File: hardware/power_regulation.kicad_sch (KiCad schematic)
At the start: 19 parts, among them U3 MAX6106, U4 LM27761

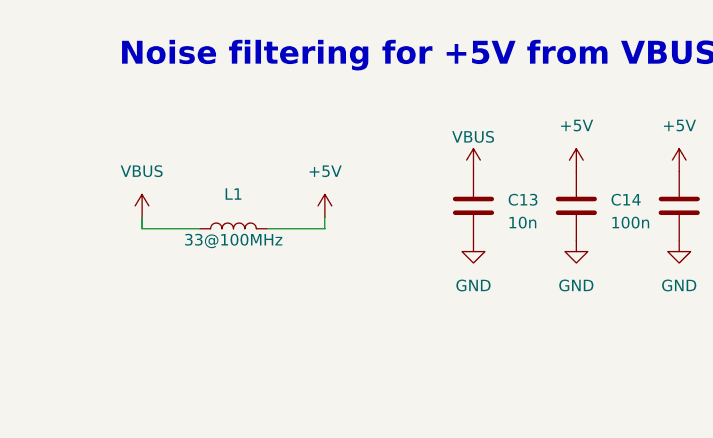
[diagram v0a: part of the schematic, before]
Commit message: finalize pcb design; add layout file
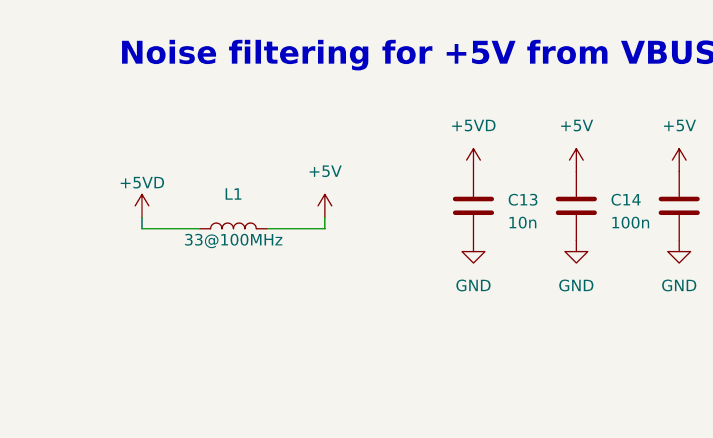
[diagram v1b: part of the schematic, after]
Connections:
- net VBUS renamed +5VD
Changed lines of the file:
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@@
   (title_block
     (title "Power regulation")
-    (date "2023-08-08")
+    (date "2023-08-15")
     (company "bitgloo")
     (comment 1 "Released under the CERN Open Hardware Licence Version 2 - Strongly Reciprocal")
@@
     )
   )
-  (symbol (lib_id "power:VBUS") (at 96.52 66.04 0) (unit 1)
-    (in_bom yes) (on_board yes) (dnp no) (fields_autoplaced)
-    (property "Reference" "#PWR061" (at 96.52 69.85 0)
-      (effects (font (size 1.27 1.27)) hide)
-    )
-    (property "Value" "VBUS" (at 96.52 62.23 0)
-      (effects (font (size 1.27 1.27)))
-    )
-    (property "Footprint" "" (at 96.52 66.04 0)
-      (effects (font (size 1.27 1.27)) hide)
-    )
-    (property "Datasheet" "" (at 96.52 66.04 0)
-      (effects (font (size 1.27 1.27)) hide)
-    )
-    (pin "1")
-    (instances
-      (project "DSP PAW add-on board"
-        (path "/c291319b-d76e-4fda-91cc-061acff65f9f/270d19d2-3af2-41db-ad1c-33373417ec82"
-          (reference "#PWR061") (unit 1)
-        )
-        (path "/c291319b-d76e-4fda-91cc-061acff65f9f/97fc232a-dbc7-49da-a6a0-e33e9aacbabd"
-          (reference "#PWR017") (unit 1)
-        )
-      )
-    )
-  )
   (symbol (lib_id "power:VDDA") (at 222.25 134.62 0) (unit 1)
     (in_bom yes) (on_board yes) (dnp no) (fields_autoplaced)
@@
         (path "/c291319b-d76e-4fda-91cc-061acff65f9f/97fc232a-dbc7-49da-a6a0-e33e9aacbabd"
           (reference "TP3") (unit 1)
-        )
-      )
-    )
-  )
-  (symbol (lib_id "power:VBUS") (at 59.69 71.12 0) (unit 1)
-    (in_bom yes) (on_board yes) (dnp no)
-    (property "Reference" "#PWR022" (at 59.69 74.93 0)
-      (effects (font (size 1.27 1.27)) hide)
-    )
-    (property "Value" "VBUS" (at 59.69 66.04 0)
-      (effects (font (size 1.27 1.27)))
-    )
-    (property "Footprint" "" (at 59.69 71.12 0)
-      (effects (font (size 1.27 1.27)) hide)
-    )
-    (property "Datasheet" "" (at 59.69 71.12 0)
-      (effects (font (size 1.27 1.27)) hide)
-    )
-    (pin "1")
-    (instances
-      (project "DSP PAW add-on board"
-        (path "/c291319b-d76e-4fda-91cc-061acff65f9f/97fc232a-dbc7-49da-a6a0-e33e9aacbabd"
-          (reference "#PWR022") (unit 1)
         )
       )
@@
     )
   )
+  (symbol (lib_id "power:+5VD") (at 96.52 66.04 0) (unit 1)
+    (in_bom yes) (on_board yes) (dnp no)
+    (property "Reference" "#PWR017" (at 96.52 69.85 0)
+      (effects (font (size 1.27 1.27)) hide)
+    )
+    (property "Value" "+5VD" (at 96.52 60.96 0)
+      (effects (font (size 1.27 1.27)))
+    )
+    (property "Footprint" "" (at 96.52 66.04 0)
+      (effects (font (size 1.27 1.27)) hide)
+    )
+    (property "Datasheet" "" (at 96.52 66.04 0)
+      (effects (font (size 1.27 1.27)) hide)
+    )
+    (pin "1")
+    (instances
+      (project "DSP PAW add-on board"
+        (path "/c291319b-d76e-4fda-91cc-061acff65f9f/97fc232a-dbc7-49da-a6a0-e33e9aacbabd"
+          (reference "#PWR017") (unit 1)
+        )
+      )
+    )
+  )
   (symbol (lib_id "power:+5V") (at 198.12 64.77 0) (unit 1)
     (in_bom yes) (on_board yes) (dnp no) (fields_autoplaced)
@@
         )
       )
+    )
+  )
+  (symbol (lib_id "power:+5VD") (at 59.69 71.12 0) (unit 1)
+    (in_bom yes) (on_board yes) (dnp no) (fields_autoplaced)
+    (property "Reference" "#PWR022" (at 59.69 74.93 0)
+      (effects (font (size 1.27 1.27)) hide)
+    )
+    (property "Value" "+5VD" (at 59.69 67.31 0)
+      (effects (font (size 1.27 1.27)))
+    )
+    (property "Footprint" "" (at 59.69 71.12 0)
+      (effects (font (size 1.27 1.27)) hide)
+    )
+    (property "Datasheet" "" (at 59.69 71.12 0)
+      (effects (font (size 1.27 1.27)) hide)
+    )
+    (pin "1")
+    (instances
+      (project "DSP PAW add-on board"
+        (path "/c291319b-d76e-4fda-91cc-061acff65f9f/97fc232a-dbc7-49da-a6a0-e33e9aacbabd"
+          (reference "#PWR022") (unit 1)
+        )
+      )

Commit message: pcb design finalization
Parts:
- C13: LCSC Part # (none) -> C57112
- C14: LCSC Part # (none) -> C14663
- C15, C16, C18, C21: LCSC Part # (none) -> C19666
- C17, C20: LCSC Part # (none) -> C15849
- C19: LCSC Part # (none) -> C23630
- L1: LCSC Part # (none) -> C88984
- R19: value 174k -> 174k/1%; LCSC Part # (none) -> C482778
- R20: LCSC Part # (none) -> C21189
- R21: value 56k -> 56k/1%; LCSC Part # (none) -> C5140721
- TP1, TP2, TP3, TP4: DNP (none) -> T
- U3: LCSC Part # (none) -> C26804; Part Number MAX6106EUR+T -> REF3020AIDBZR
- U4: LCSC Part # (none) -> C129351
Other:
- note added: "Can substitute REF3020"
- title: Power regulation -> DSP PAW add-on board
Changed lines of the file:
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@@
   (paper "A4")
   (title_block
-    (title "Power regulation")
-    (date "2023-08-15")
+    (title "DSP PAW add-on board")
+    (date "2023-08-18")
     (company "bitgloo")
     (comment 1 "Released under the CERN Open Hardware Licence Version 2 - Strongly Reciprocal")
@@
     (effects (font (size 2.54 2.54) (thickness 0.254) bold) (justify left bottom))
   )
+  (text "Can substitute REF3020" (at 170.18 78.74 0)
+    (effects (font (size 1.27 1.27)) (justify left bottom))
+  )
   (text "Noise filtering for +5V from VBUS" (at 57.15 54.61 0)
     (effects (font (size 2.54 2.54) (thickness 0.254) bold) (justify left bottom))
@@
       (effects (font (size 1.27 1.27)) hide)
     )
+    (property "DNP" "T" (at 204.47 134.62 0)
+      (effects (font (size 1.27 1.27)) hide)
+    )
+    (property "LCSC Part #" "" (at 204.47 134.62 0)
+      (effects (font (size 1.27 1.27)) hide)
+    )
     (pin "1")
     (instances
@@
     )
     (property "Part Number" "CL10A475KP8NNNC" (at 118.11 135.89 0)
+      (effects (font (size 1.27 1.27)) hide)
+    )
+    (property "DNP" "" (at 118.11 135.89 0)
+      (effects (font (size 1.27 1.27)) hide)
+    )
+    (property "LCSC Part #" "C19666" (at 118.11 135.89 0)
       (effects (font (size 1.27 1.27)) hide)
     )
@@
       (effects (font (size 1.27 1.27)) hide)
     )
+    (property "DNP" "" (at 63.5 142.24 0)
+      (effects (font (size 1.27 1.27)) hide)
+    )
+    (property "LCSC Part #" "C15849" (at 63.5 142.24 0)
+      (effects (font (size 1.27 1.27)) hide)
+    )
     (pin "1")
     (pin "2")
@@
       (effects (font (size 1.27 1.27)) hide)
     )
+    (property "DNP" "T" (at 231.14 135.89 0)
+      (effects (font (size 1.27 1.27)) hide)
+    )
+    (property "LCSC Part #" "" (at 231.14 135.89 0)
+      (effects (font (size 1.27 1.27)) hide)
+    )
     (pin "1")
     (instances
@@
     )
     (property "Part Number" "CL10B105KP8NNNC" (at 242.57 72.39 0)
+      (effects (font (size 1.27 1.27)) hide)
+    )
+    (property "DNP" "" (at 242.57 72.39 0)
+      (effects (font (size 1.27 1.27)) hide)
+    )
+    (property "LCSC Part #" "C15849" (at 242.57 72.39 0)
       (effects (font (size 1.27 1.27)) hide)
     )
@@
       (effects (font (size 1.27 1.27) italic) hide)
     )
-    (property "Part Number" "MAX6106EUR+T" (at 200.66 72.39 0)
+    (property "Part Number" "REF3020AIDBZR" (at 200.66 72.39 0)
+      (effects (font (size 1.27 1.27)) hide)
+    )
+    (property "DNP" "" (at 200.66 72.39 0)
+      (effects (font (size 1.27 1.27)) hide)
+    )
+    (property "LCSC Part #" "C26804" (at 200.66 72.39 0)
       (effects (font (size 1.27 1.27)) hide)
     )
@@
       (effects (font (size 1.27 1.27)) (justify left))
     )
-    (property "Value" "174k" (at 105.41 132.715 0)
+    (property "Value" "174k/1%" (at 105.41 132.715 0)
       (effects (font (size 1.27 1.27)) (justify left))
     )
@@
       (effects (font (size 1.27 1.27)) hide)
     )
+    (property "DNP" "" (at 102.87 130.81 0)
+      (effects (font (size 1.27 1.27)) hide)
+    )
+    (property "LCSC Part #" "C482778" (at 102.87 130.81 0)
+      (effects (font (size 1.27 1.27)) hide)
+    )
     (pin "1")
     (pin "2")
@@
     )
     (property "Part Number" "CL10A475KP8NNNC" (at 91.44 144.78 0)
+      (effects (font (size 1.27 1.27)) hide)
+    )
+    (property "DNP" "" (at 91.44 144.78 0)
+      (effects (font (size 1.27 1.27)) hide)
+    )
+    (property "LCSC Part #" "C19666" (at 91.44 144.78 0)
       (effects (font (size 1.27 1.27)) hide)
     )
@@
       (effects (font (size 1.27 1.27)) hide)
     )
+    (property "DNP" "T" (at 213.36 134.62 0)
+      (effects (font (size 1.27 1.27)) hide)
+    )
+    (property "LCSC Part #" "" (at 213.36 134.62 0)
+      (effects (font (size 1.27 1.27)) hide)
+    )
     (pin "1")
     (instances
@@
       (effects (font (size 1.27 1.27)) hide)
     )
+    (property "DNP" "" (at 130.81 135.89 0)
+      (effects (font (size 1.27 1.27)) hide)
+    )
+    (property "LCSC Part #" "C23630" (at 130.81 135.89 0)
+      (effects (font (size 1.27 1.27)) hide)
+    )
     (pin "1")
     (pin "2")
@@
       (effects (font (size 1.27 1.27)) hide)
     )
+    (property "DNP" "" (at 55.88 133.35 0)
+      (effects (font (size 1.27 1.27)) hide)
+    )
+    (property "LCSC Part #" "C21189" (at 55.88 133.35 0)
+      (effects (font (size 1.27 1.27)) hide)
+    )
     (pin "1")
     (pin "2")
@@
     )
     (property "Part Number" "CL10A475KP8NNNC" (at 229.87 72.39 0)
+      (effects (font (size 1.27 1.27)) hide)
+    )
+    (property "DNP" "" (at 229.87 72.39 0)
+      (effects (font (size 1.27 1.27)) hide)
+    )
+    (property "LCSC Part #" "C19666" (at 229.87 72.39 0)
       (effects (font (size 1.27 1.27)) hide)
     )
@@
       (effects (font (size 1.27 1.27)) hide)
     )
+    (property "DNP" "T" (at 222.25 134.62 0)
+      (effects (font (size 1.27 1.27)) hide)
+    )
+    (property "LCSC Part #" "" (at 222.25 134.62 0)
+      (effects (font (size 1.27 1.27)) hide)
+    )
     (pin "1")
     (instances
@@
       (effects (font (size 1.27 1.27)) hide)
     )
+    (property "DNP" "" (at 119.38 69.85 0)
+      (effects (font (size 1.27 1.27)) hide)
+    )
+    (property "LCSC Part #" "C19666" (at 119.38 69.85 0)
+      (effects (font (size 1.27 1.27)) hide)
+    )
     (pin "1")
     (pin "2")
@@
       (effects (font (size 1.27 1.27)) (justify left))
     )
-    (property "Value" "56k" (at 105.41 142.875 0)
+    (property "Value" "56k/1%" (at 105.41 142.875 0)
       (effects (font (size 1.27 1.27)) (justify left))
     )
@@
       (effects (font (size 1.27 1.27)) hide)
     )
+    (property "DNP" "" (at 102.87 140.97 0)
+      (effects (font (size 1.27 1.27)) hide)
+    )
+    (property "LCSC Part #" "C5140721" (at 102.87 140.97 0)
+      (effects (font (size 1.27 1.27)) hide)
+    )
     (pin "1")
     (pin "2")
@@
     )
     (property "Part Number" "CL10B104KB8NNWC" (at 107.95 69.85 0)
+      (effects (font (size 1.27 1.27)) hide)
+    )
+    (property "DNP" "" (at 107.95 69.85 0)
+      (effects (font (size 1.27 1.27)) hide)
+    )
+    (property "LCSC Part #" "C14663" (at 107.95 69.85 0)
       (effects (font (size 1.27 1.27)) hide)
     )
@@
     )
     (property "Part Number" "LM27761DSGR" (at 77.47 138.43 0)
+      (effects (font (size 1.27 1.27)) hide)
+    )
+    (property "DNP" "" (at 77.47 138.43 0)
+      (effects (font (size 1.27 1.27)) hide)
+    )
+    (property "LCSC Part #" "C129351" (at 77.47 138.43 0)
       (effects (font (size 1.27 1.27)) hide)
     )
@@
       (effects (font (size 1.27 1.27)) hide)
     )
+    (property "DNP" "" (at 69.85 72.39 0)
+      (effects (font (size 1.27 1.27)) hide)
+    )
+    (property "LCSC Part #" "C88984" (at 69.85 72.39 0)
+      (effects (font (size 1.27 1.27)) hide)
+    )
     (pin "1")
     (pin "2")
@@
       (effects (font (size 1.27 1.27)) hide)
     )
+    (property "DNP" "" (at 96.52 69.85 0)
+      (effects (font (size 1.27 1.27)) hide)
+    )
+    (property "LCSC Part #" "C57112" (at 96.52 69.85 0)
+      (effects (font (size 1.27 1.27)) hide)
+    )
